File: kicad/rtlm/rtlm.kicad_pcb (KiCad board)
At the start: 4 copper layers, 200 x 110 mm, 265 parts, among them IC1 ESP32-S3FN8, IC2 TPS25940ARVCR, IC3 PE4259, IC4 TPS2553DBVR, IC5 TLV9004IDR, IC6 TLV9004IDR, IC7 TCAN1042HGVDR, IC8 TPS2553DBVR, IC9 TLC59116IPWR, J1 USB_C_Receptacle_USB2.0_16P, J10 TEMP_2, J11 TEMP_3, J12 TEMP_4, J13 ANALOG_1, J14 ANALOG_2, J15 ANALOG_3, J16 ANALOG_4, J17 DM3AT-SF-PEJM5, J18 CAN_EXPANSION, J19 BATTERY_VOLTAGE_SENSE_LINE, J2 Conn_01x02, J3 UART_DEBUG_3V3, J4 LORA_ANT, J5 PULSE_1, J6 PULSE_2, J7 PULSE_3, J8 PULSE_4, J9 TEMP_1, Q1 DMP2035U-7, SW1 SW_Push, SW2 SW_Push, U1 TPS62130A, U10 RV-3028-C7, U2 TPS2116DRL, U3 TPD2EUSB30, U4 SX1262IMLTRT, U5 SN74LVC14ADR, U6 MCP3208-BI/SL, U7 REF3025AIDBZR, U8 AMC3330, U9 ADS1115IDGS, Y1 40MHz, Y2 TG2520SMN 32.0000M-MCGNNM3

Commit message: fix: remove stray traces
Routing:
- net GND: track 51.4 -> 50.8 mm
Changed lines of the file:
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@@
-	)
-	(segment
-		(start 217 194.19636)
-		(end 217 193.67)
-		(width 0.2)
-		(layer "F.Cu")
-		(net "GND")
 	)
 	(segment
@@
 		(width 0.2)
 		(layer "F.Cu")
-		(net "GND")
-	)
-	(segment
-		(start 217 193.67)
-		(end 216.99 193.66)
-		(width 0.2)
-		(layer "F.Cu")

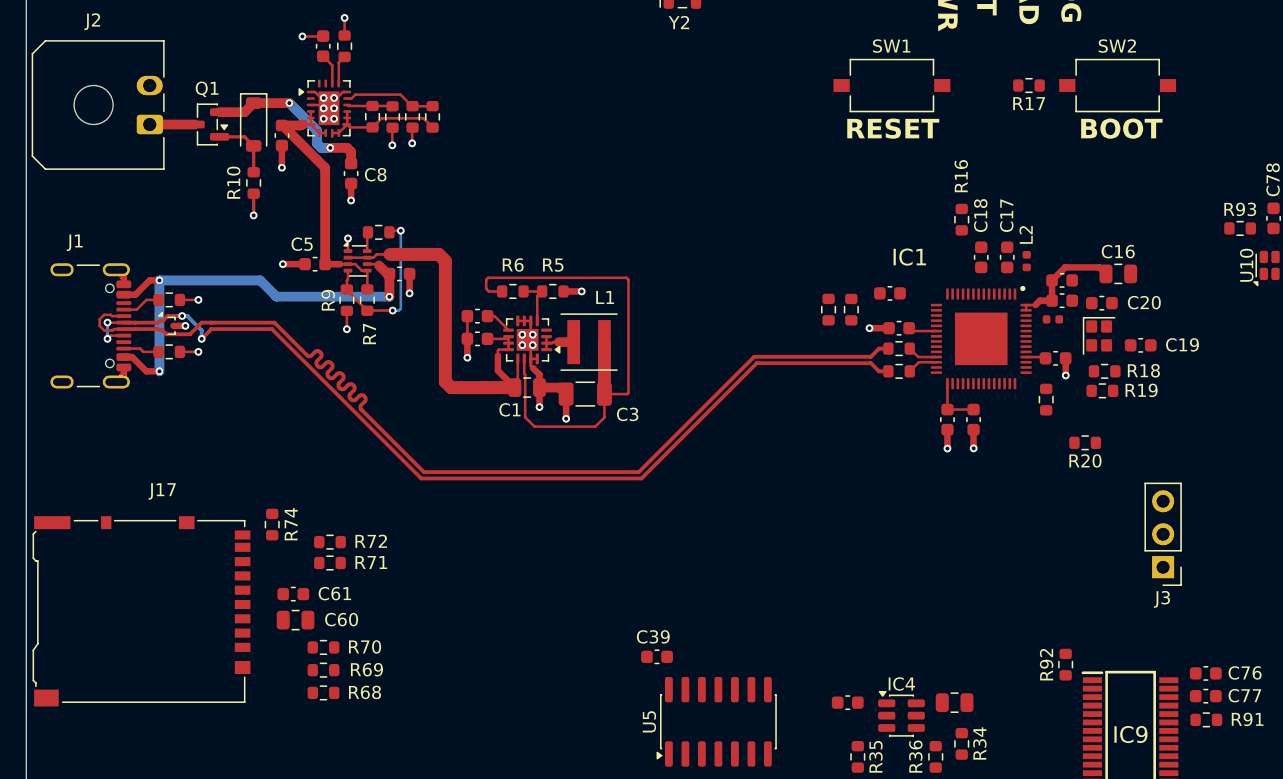
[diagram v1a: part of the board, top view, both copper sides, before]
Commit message: feat: start IC1 routing, SD, and UART; fix misnamed UART label
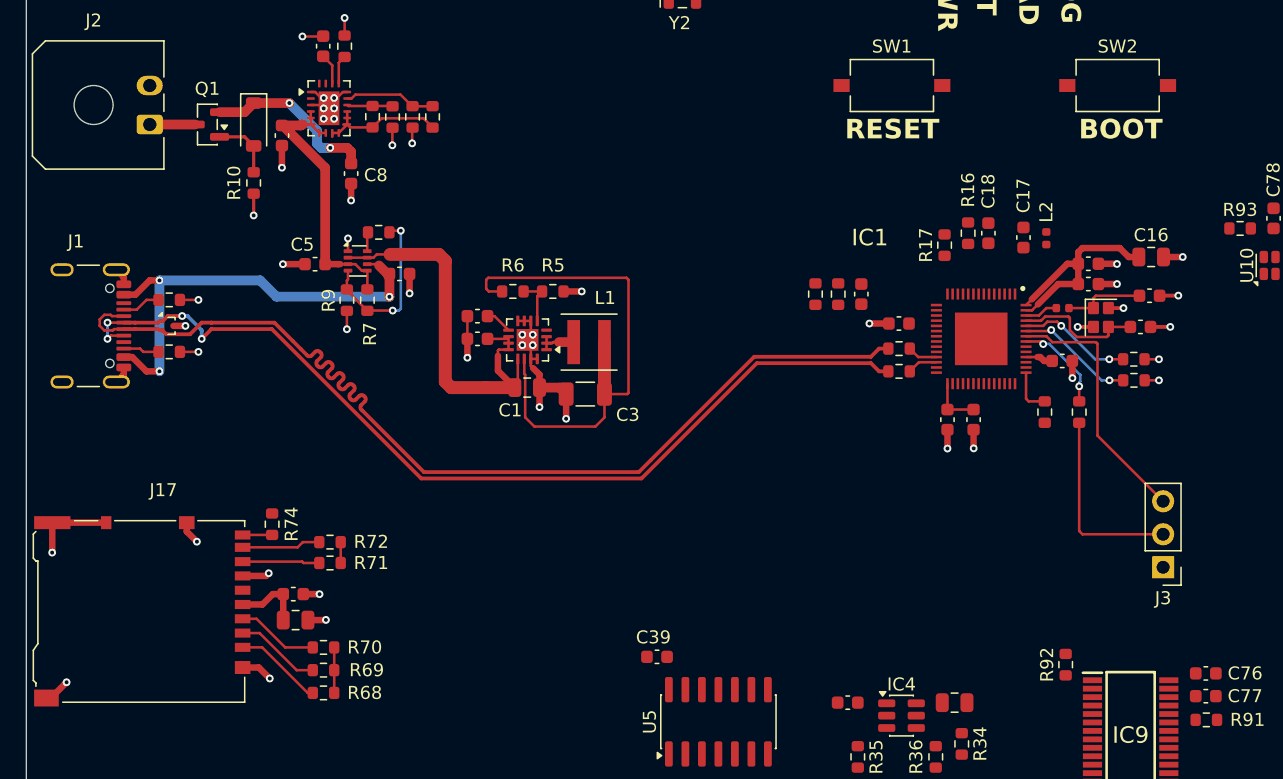
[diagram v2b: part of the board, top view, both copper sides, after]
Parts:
- moved R17 13.9 mm to (265.2, 203.8), turned to 90 degrees
- moved C20 3.71 mm to (281.0, 207.7)
- moved C16 2.84 mm to (281.1, 204.7)
- moved R19 2.56 mm to (279.8, 214.2)
- moved R18 2.43 mm to (279.7, 212.6)
- moved R20 2.41 mm to (275.5, 216.6), turned to 90 degrees
- moved C14 2.39 mm to (276.2, 206.8)
- moved C15 2.39 mm to (276.2, 205.2)
- moved L2 2.32 mm to (273.0, 203.3)
- moved C59 2.21 mm to (258.8, 207.6), turned to -90 degrees
- moved C17 1.97 mm to (271.2, 203.2)
- moved C18 1.94 mm to (268.6, 202.9)
- moved R66 1.56 mm to (255.2, 207.6)
- moved R67 1.56 mm to (257.0, 207.6)
- moved Y1 1.43 mm to (277.2, 209.4)
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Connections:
- IC1 pad 53: /ESP_XTAL_P -> /ESP_XTAL_N
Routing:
- net GND: track 50.8 -> 80.2 mm, vias 32 -> 48
- net /ESP_U0RXD: track 0.00 -> 20.0 mm
- net +3.3V: track 53.3 -> 71.1 mm
- net Net-(J3-Pin_2): track 0.00 -> 14.9 mm
- net /ESP_XTAL_N: track 0.00 -> 10.1 mm
- net Net-(IC1-GPIO45): track 0.00 -> 9.12 mm, vias 0 -> 2
- net Net-(IC1-GPIO46): track 0.00 -> 8.80 mm, vias 0 -> 2
- net /ESP_U0TXD: track 0.00 -> 7.32 mm, vias 0 -> 2
- net /SD_D2: track 0.00 -> 6.85 mm
- net /SD_D3: track 0.00 -> 6.58 mm
- net /SD_CMD: track 0.00 -> 6.31 mm
- net Net-(C20-Pad2): track 0.00 -> 6.27 mm
- net /SD_D1: track 0.00 -> 6.07 mm
- net /SD_D0: track 0.00 -> 5.94 mm
- net Net-(IC1-GPIO38): track 0.00 -> 3.53 mm
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
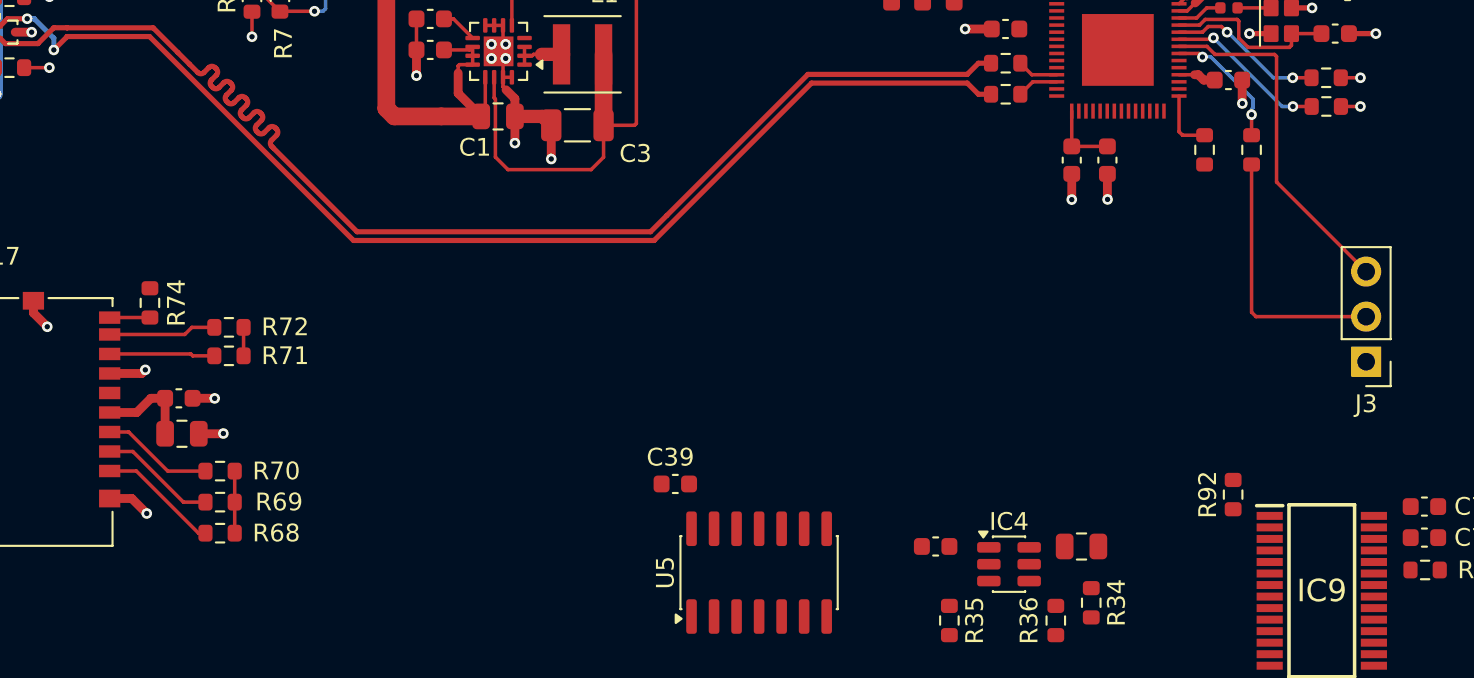
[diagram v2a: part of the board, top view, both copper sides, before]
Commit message: feat: SD routing, incomplete IC1 side.
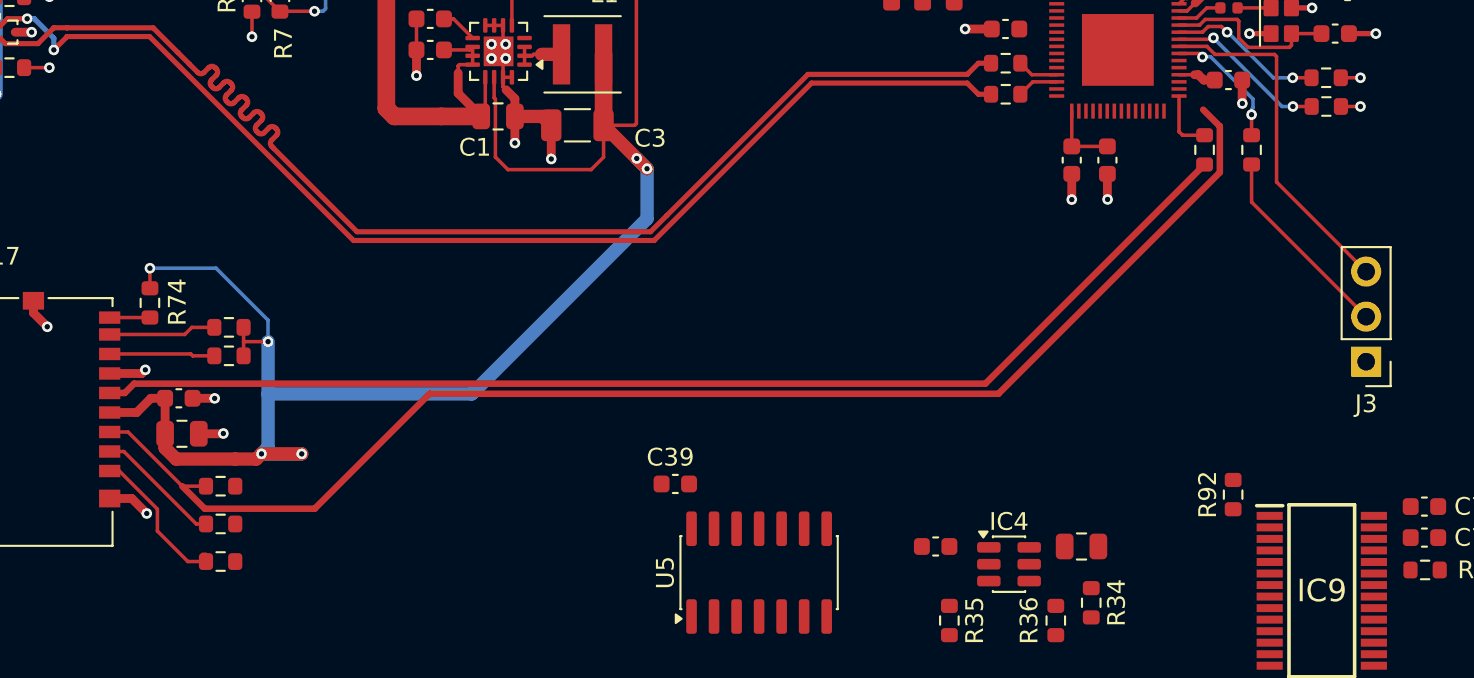
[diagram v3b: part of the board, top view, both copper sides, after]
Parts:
- moved R68 1.60 mm to (217.4, 239.8)
- moved R69 1.23 mm to (217.4, 237.7)
- moved R70 0.85 mm to (217.4, 235.6)
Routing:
- net /SD_CMD: track 6.31 -> 77.5 mm
- net /SD_CLK: track 0.00 -> 67.1 mm
- net +3.3V: track 71.1 -> 129.4 mm, vias 0 -> 6
- net Net-(J3-Pin_2): track 14.9 -> 11.3 mm
- net /SD_D2: track 6.85 -> 8.46 mm
- net /SD_D3: track 6.58 -> 7.12 mm

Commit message: feat: finish prelim SD routing, TODO tunings
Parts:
- moved C11 1.89 mm to (276.0, 213.4)
- moved L3 0.54 mm to (274.5, 208.2)
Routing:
- net /SD_D2: track 8.46 -> 92.7 mm, vias 0 -> 2
- net /SD_D3: track 7.12 -> 82.3 mm, vias 0 -> 2
- net /SD_D0: track 5.94 -> 76.8 mm, vias 0 -> 2
- net /SD_D1: track 6.07 -> 75.5 mm, vias 0 -> 2
- net /SD_DETECT: track 2.27 -> 59.3 mm
- net +3.3V: track 129.4 -> 141.8 mm, vias 6 -> 9
- net /ESP_U0RXD: track 20.0 -> 24.2 mm
- net /SD_CMD: track 77.5 -> 80.0 mm
- net /ESP_U0TXD: track 7.32 -> 8.67 mm
- net Net-(IC1-GPIO45): track 9.12 -> 10.3 mm
- net Net-(IC1-GPIO46): track 8.80 -> 9.40 mm
- net GND: track 80.2 -> 80.8 mm
- added copper zone on In2.Cu, net GND

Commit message: fix: prelim tuning of SD data lines
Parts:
- moved U5 2.10 mm to (247.1, 242.5)
- moved C39 2.10 mm to (242.4, 237.5)
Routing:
- net /SD_CLK: track 67.1 -> 90.0 mm
- net /SD_CMD: track 80.0 -> 96.6 mm
- net /SD_D1: track 75.5 -> 87.2 mm
- net /SD_D3: track 82.3 -> 93.8 mm
- net /SD_D0: track 76.8 -> 87.3 mm
- net /SD_D2: track 92.7 -> 95.3 mm

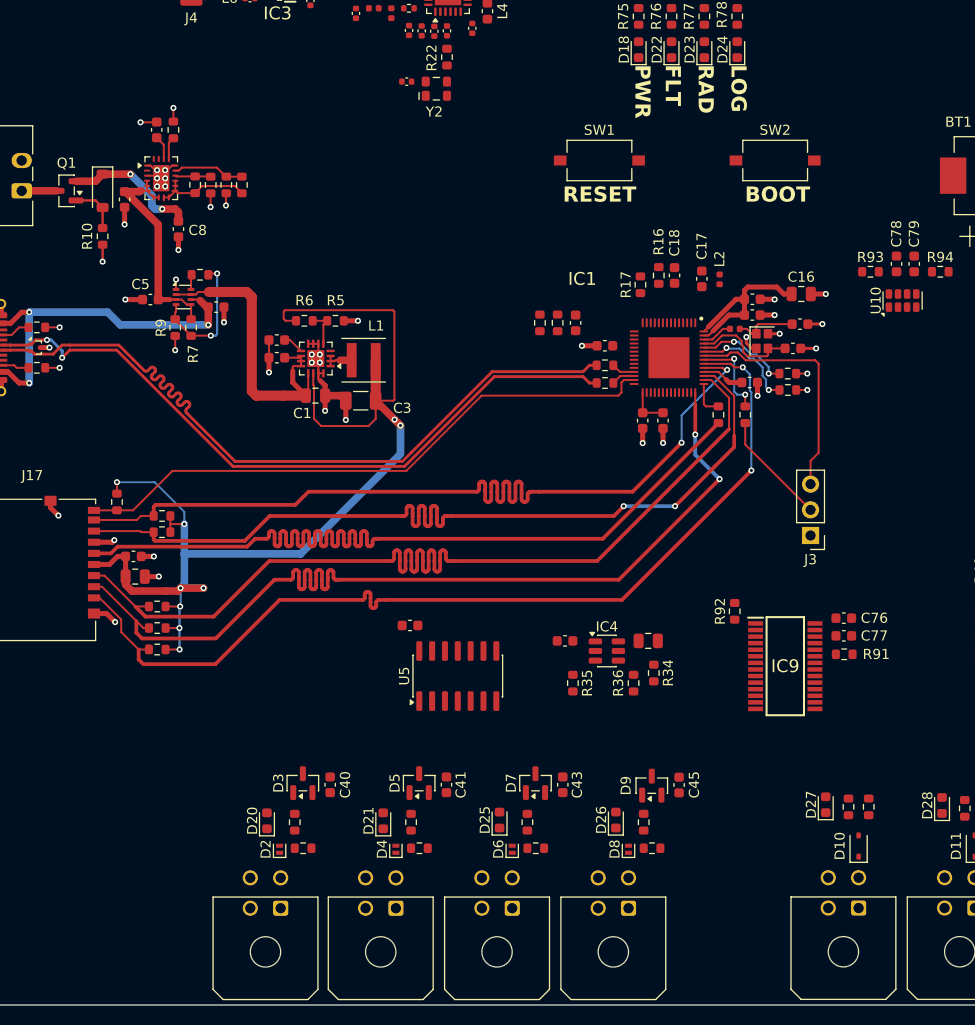
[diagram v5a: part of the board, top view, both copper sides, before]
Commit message: feat: finish pulse routing, start status LED routing
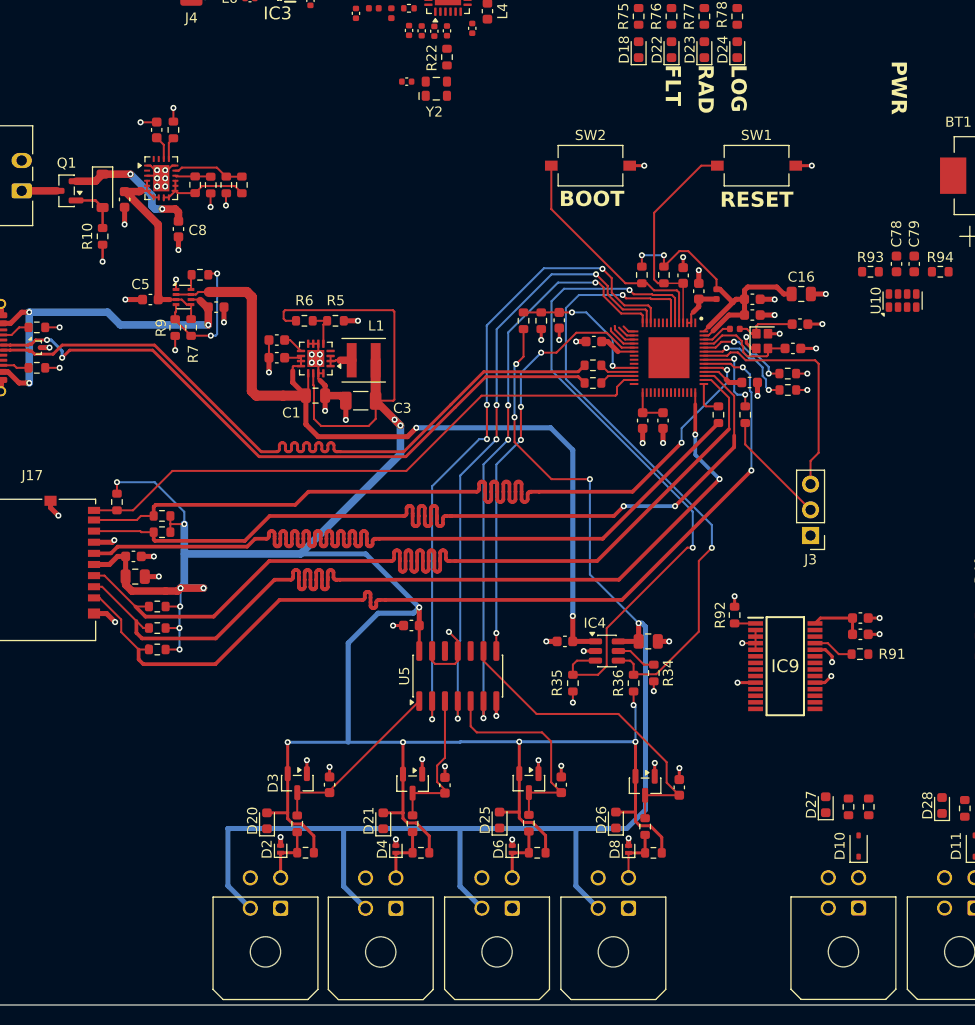
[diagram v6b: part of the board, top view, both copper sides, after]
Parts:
- moved SW2 18.3 mm to (260.2, 192.0)
- moved SW1 15.5 mm to (276.7, 192.0)
- moved R32 3.18 mm to (266.5, 260.0), turned to 0 degrees
- moved R33 2.25 mm to (265.6, 257.4), turned to 90 degrees
- moved C77 1.64 mm to (286.9, 238.3)
- moved C59 1.64 mm to (257.1, 207.3)
- moved C76 1.64 mm to (286.9, 236.7)
- moved R66 1.63 mm to (253.6, 207.3)
- moved R67 1.63 mm to (255.4, 207.3)
- moved R91 1.56 mm to (286.9, 240.3)
- moved L2 1.49 mm to (272.7, 204.7)
- moved C17 1.26 mm to (270.9, 204.4)
- moved R3 1.19 mm to (260.5, 211.8)
- moved R4 1.19 mm to (260.5, 213.5)
- moved C10 1.17 mm to (260.6, 209.4)
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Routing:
- net +3.3V: track 141.8 -> 299.6 mm, vias 9 -> 17
- net /5V_PULSE: track 0.00 -> 136.7 mm, vias 0 -> 4
- net /PULSE_PWR_EN: track 0.00 -> 68.3 mm, vias 0 -> 2
- net /PULSE_1: track 0.00 -> 65.9 mm, vias 0 -> 4
- net /SENSOR_PWR_FAULT: track 0.00 -> 62.8 mm, vias 0 -> 2
- net /PULSE_2: track 0.00 -> 62.1 mm, vias 0 -> 4
- net /PULSE_3: track 0.00 -> 58.8 mm, vias 0 -> 4
- net /5V_SYS: track 31.5 -> 83.7 mm, vias 0 -> 2
- net GND: track 80.8 -> 128.2 mm, vias 48 -> 81
- net /PULSE_4: track 0.00 -> 41.9 mm, vias 0 -> 4
- net Net-(D9-COM): track 0.00 -> 32.7 mm
- net /ESP_BOOT: track 0.00 -> 23.3 mm
- net Net-(D7-COM): track 0.00 -> 21.9 mm
- net /ESP_RESET: track 0.00 -> 21.7 mm
- net Net-(D3-COM): track 0.00 -> 18.2 mm
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
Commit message: feat: power planing
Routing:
- net +3.3V: track 299.6 -> 302.2 mm
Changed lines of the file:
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@@
+	)
+	(segment
+		(start 286.15 238.75)
+		(end 286.15 238.35)
+		(width 0.2)
+		(layer "F.Cu")
+		(net "+3.3V")
 	)
 	(segment
@@
 		(layer "F.Cu")
 		(net "+3.3V")
+	)
+	(segment
+		(start 287.71 240.31)
+		(end 286.15 238.75)
+		(width 0.2)
+		(layer "F.Cu")
+		(net "+3.3V")

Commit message: feat: -30$ for nada
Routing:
- net +3.3V: track 302.2 -> 805.2 mm, vias 17 -> 22
- net GND: track 128.2 -> 0.00 mm, vias 81 -> 0
- net /5V_SYS: track 83.7 -> 200.7 mm, vias 2 -> 4
- net /5V_PULSE: track 136.7 -> 249.5 mm, vias 4 -> 2
- net /SD_CMD: track 96.6 -> 6.70 mm
- net /ADC_VREF_2V5: track 0.00 -> 88.0 mm, vias 0 -> 2
- net /SD_D2: track 95.3 -> 7.97 mm, vias 2 -> 0
- net /SD_D3: track 93.8 -> 7.12 mm, vias 2 -> 0
- net /SD_D0: track 87.3 -> 5.94 mm, vias 2 -> 0
- net /SD_D1: track 87.2 -> 6.07 mm, vias 2 -> 0
- net /PULSE_PWR_EN: track 68.3 -> 0.00 mm, vias 2 -> 0
- net /PULSE_1: track 65.9 -> 0.00 mm, vias 4 -> 0
- net /SENSOR_PWR_FAULT: track 62.8 -> 0.00 mm, vias 2 -> 0
- net /PULSE_2: track 62.1 -> 0.00 mm, vias 4 -> 0
- net /SD_DETECT: track 59.2 -> 0.00 mm
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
